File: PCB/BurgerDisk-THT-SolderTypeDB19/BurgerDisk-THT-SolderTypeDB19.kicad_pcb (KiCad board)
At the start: 2 copper layers, 93.7 x 67.6 mm, 17 parts, among them J1 Daisy port in, J2 MicroSD module, J3 UART, J4 Daisy port out, U1 PC817

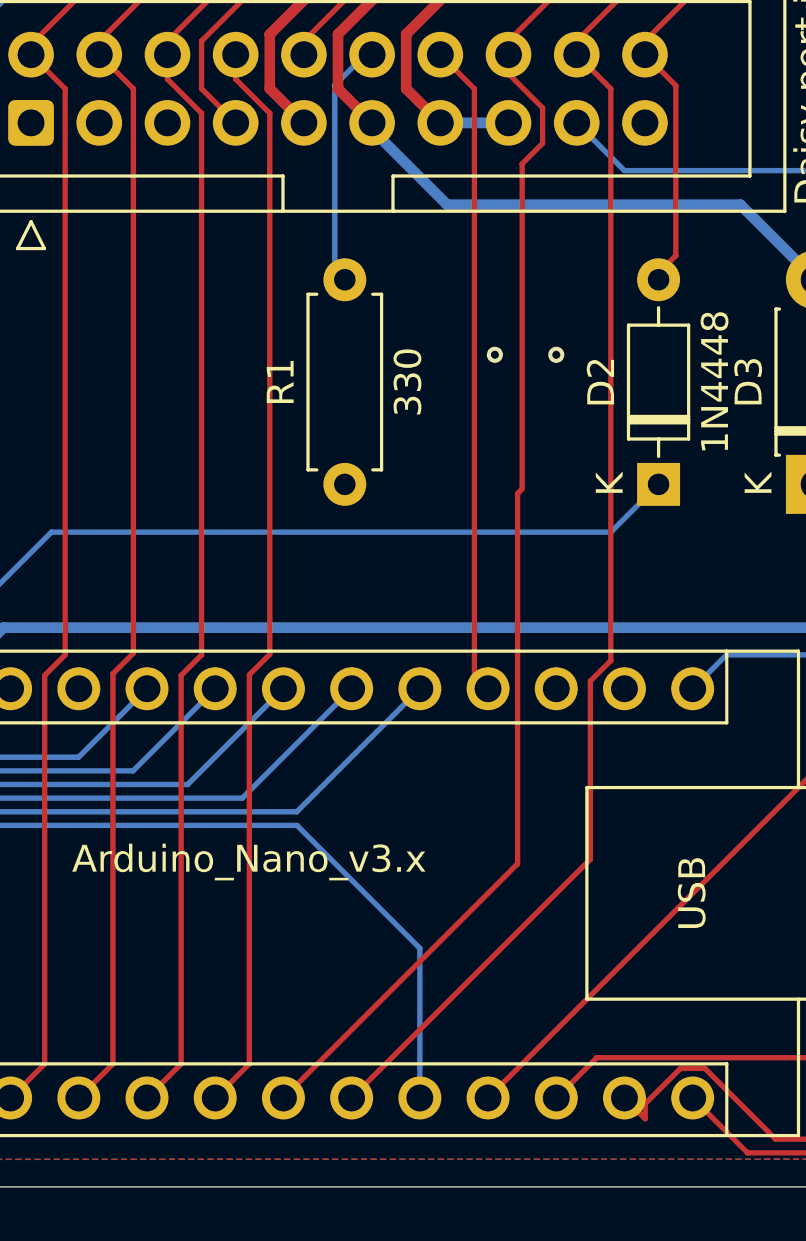
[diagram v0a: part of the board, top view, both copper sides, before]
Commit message: Cleanup PCBs, fatter power traces
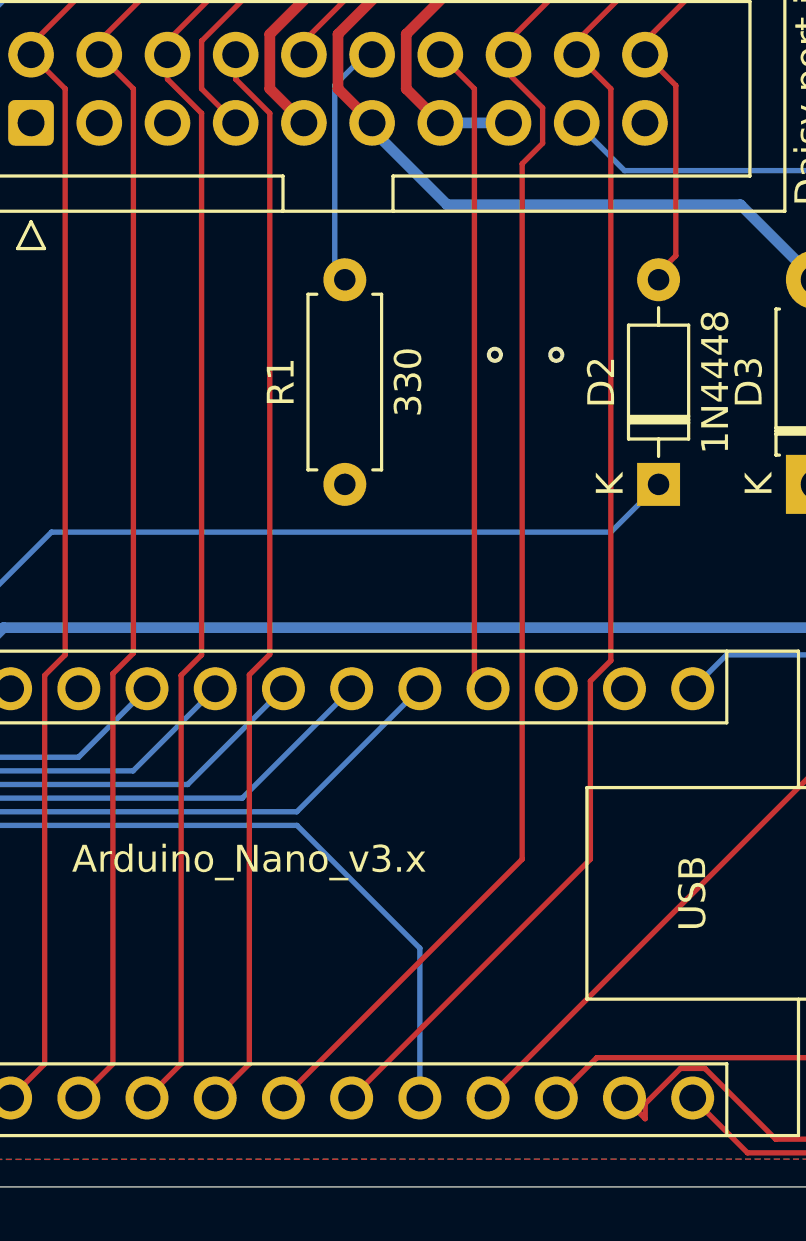
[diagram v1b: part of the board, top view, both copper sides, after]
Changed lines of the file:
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@@
+	)
+	(segment
+		(start 114.808 71.06812)
+		(end 114.808 72.39)
+		(width 0.2)
+		(layer "F.Cu")
+		(net 7)
 	)
 	(segment
@@
 	)
 	(segment
-		(start 113.876 85.428)
-		(end 113.876 99.22)
+		(start 114.046 99.05)
+		(end 105.156 107.94)
+		(width 0.2)
+		(layer "F.Cu")
+		(net 7)
+	)
+	(segment
+		(start 114.046 73.152)
+		(end 114.046 99.05)
+		(width 0.2)
+		(layer "F.Cu")
+		(net 7)
+	)
+	(segment
+		(start 122.936 59.182)
+		(end 113.538 68.58)
+		(width 0.2)
+		(layer "F.Cu")
+		(net 7)
+	)
+	(segment
+		(start 147.574 50.8)
+		(end 139.192 59.182)
+		(width 0.2)
+		(layer "F.Cu")
+		(net 7)
+	)
+	(segment
+		(start 139.192 59.182)
+		(end 122.936 59.182)
 		(width 0.2)
 		(layer "F.Cu")
@@
 	)
 	(segment
-		(start 122.936 59.182)
-		(end 113.538 68.58)
-		(width 0.2)
-		(layer "F.Cu")
-		(net 7)
-	)
-	(segment
-		(start 147.574 50.8)
-		(end 139.192 59.182)
-		(width 0.2)
-		(layer "F.Cu")
-		(net 7)
-	)
-	(segment
 		(start 113.538 69.088)
 		(end 113.538 69.79812)
-		(width 0.2)
-		(layer "F.Cu")
-		(net 7)
-	)
-	(segment
-		(start 139.192 59.182)
-		(end 122.936 59.182)
-		(width 0.2)
-		(layer "F.Cu")
-		(net 7)
-	)
-	(segment
-		(start 114.046 73.152)
-		(end 114.046 85.258)
-		(width 0.2)
-		(layer "F.Cu")
-		(net 7)
-	)
-	(segment
-		(start 114.046 85.258)
-		(end 113.876 85.428)
-		(width 0.2)
-		(layer "F.Cu")
-		(net 7)
-	)
-	(segment
-		(start 113.876 99.22)
-		(end 105.156 107.94)
-		(width 0.2)
-		(layer "F.Cu")
-		(net 7)
-	)
-	(segment
-		(start 114.808 71.06812)
-		(end 114.808 72.39)
 		(width 0.2)
 		(layer "F.Cu")
@@
 		(min_thickness 0.25)
 		(filled_areas_thickness no)
-		(fill yes
+		(fill
 			(thermal_gap 0.5)
 			(thermal_bridge_width 0.5)

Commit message: Let the OCD win
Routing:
- net WRPROT_out: track 55.9 -> 56.5 mm
- net GND: vias 4 -> 27

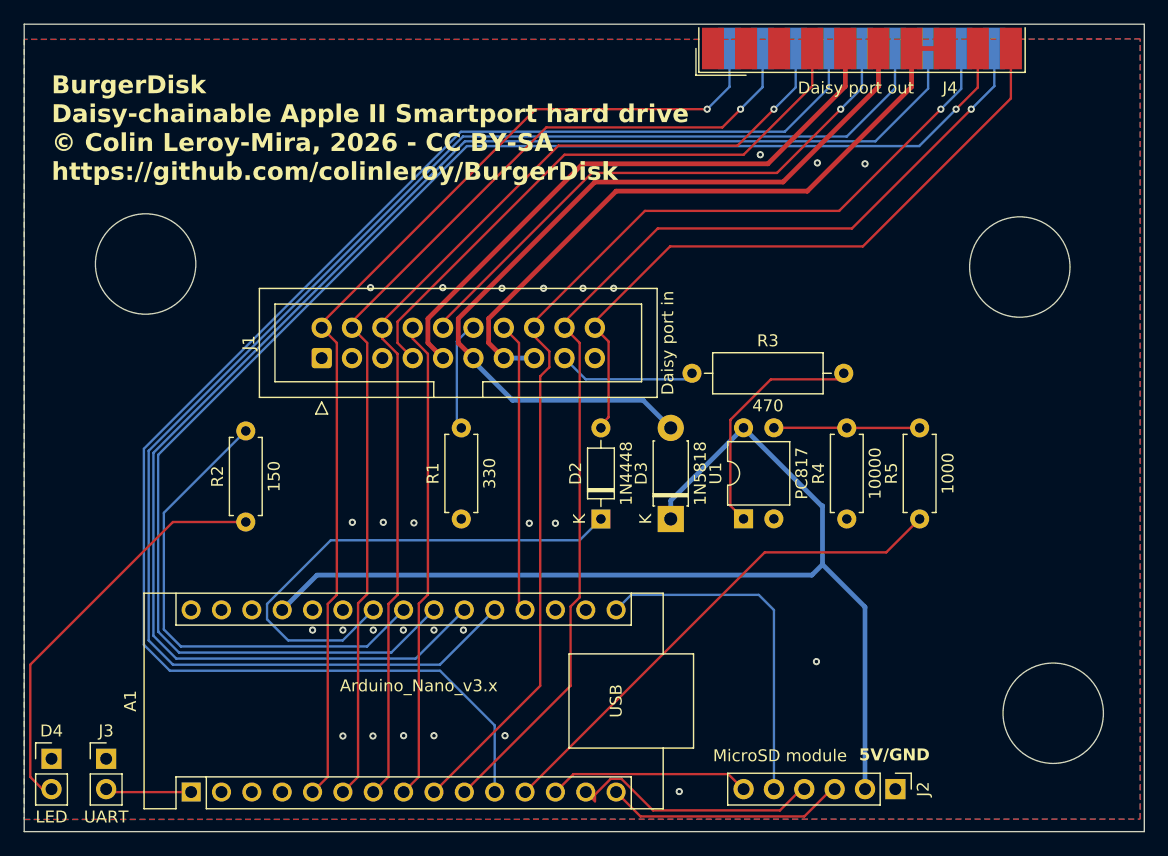
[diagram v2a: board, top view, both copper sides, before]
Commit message: Rework R3 so everything's in line
for easier soldering
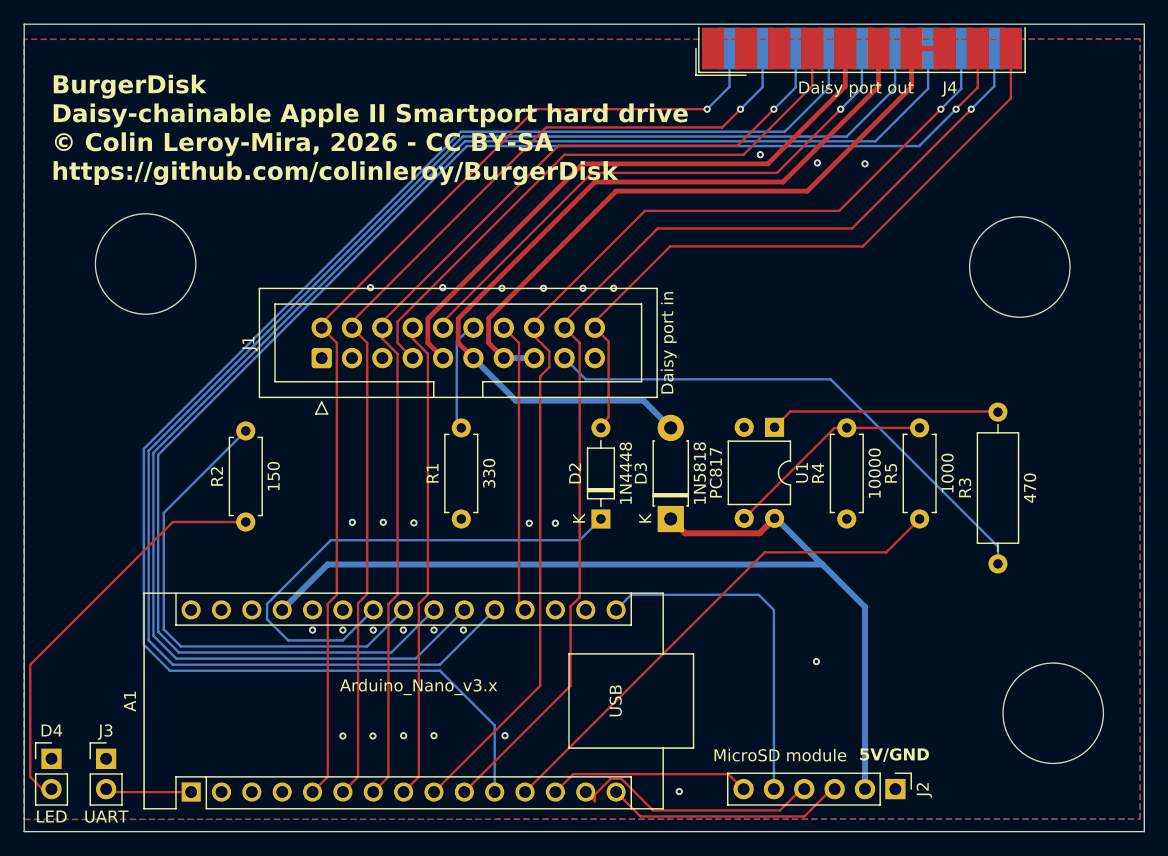
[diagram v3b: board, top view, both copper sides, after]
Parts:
- moved R3 30.2 mm to (152.3, 88.8), turned to 90 degrees
- moved U1 8.09 mm to (133.7, 77.4), turned to -90 degrees
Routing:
- net DRV2_in: track 11.6 -> 44.3 mm
- net 5V_burgerDisk: track 91.4 -> 82.3 mm
- net Net-(R4-Pad2): track 12.2 -> 17.8 mm
- net Net-(R3-Pad2): track 19.8 -> 19.3 mm

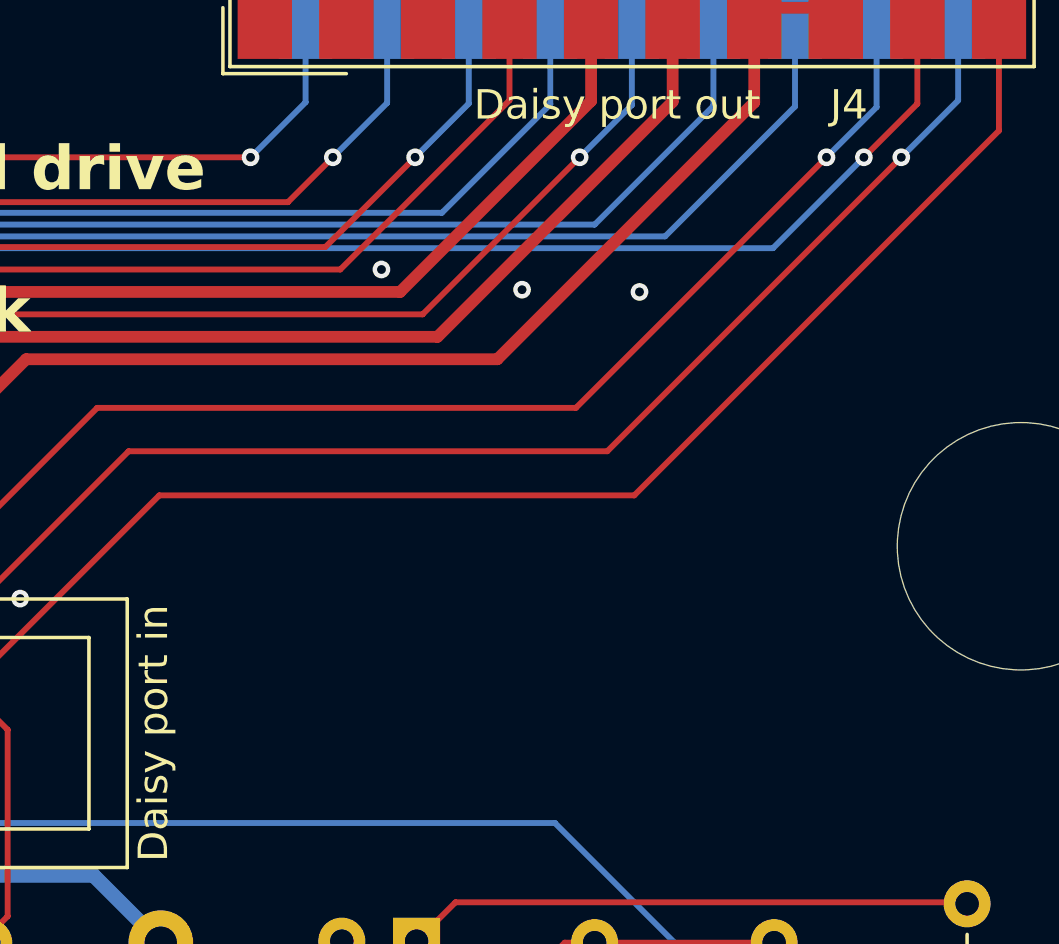
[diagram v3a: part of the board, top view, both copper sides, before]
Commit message: Add logo (thanks to Javier Rivera!!)
Add my own micro/SD modules
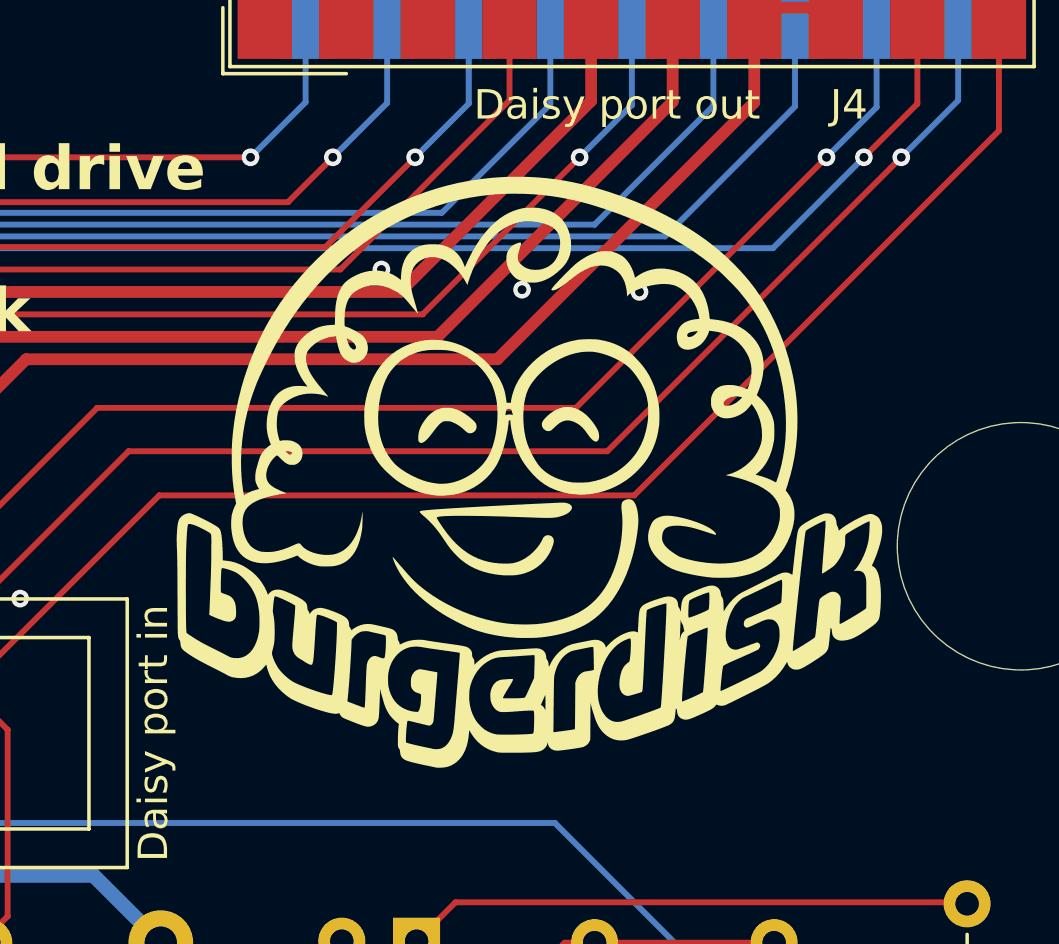
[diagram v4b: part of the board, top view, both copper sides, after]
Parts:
- added G***: LOGO, LOGO, F.Cu at (137.5, 61.6)

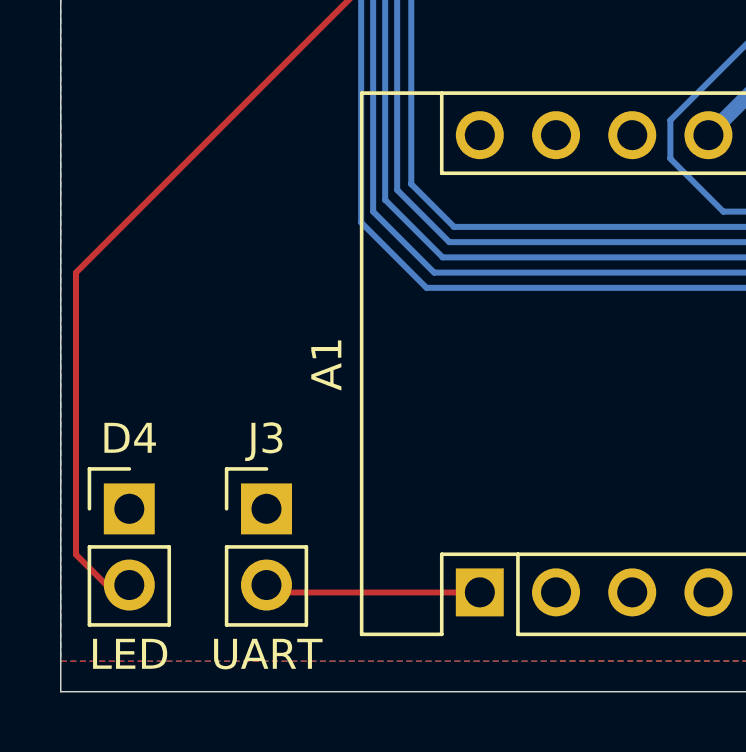
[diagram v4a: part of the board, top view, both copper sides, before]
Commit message: Small caps fixes
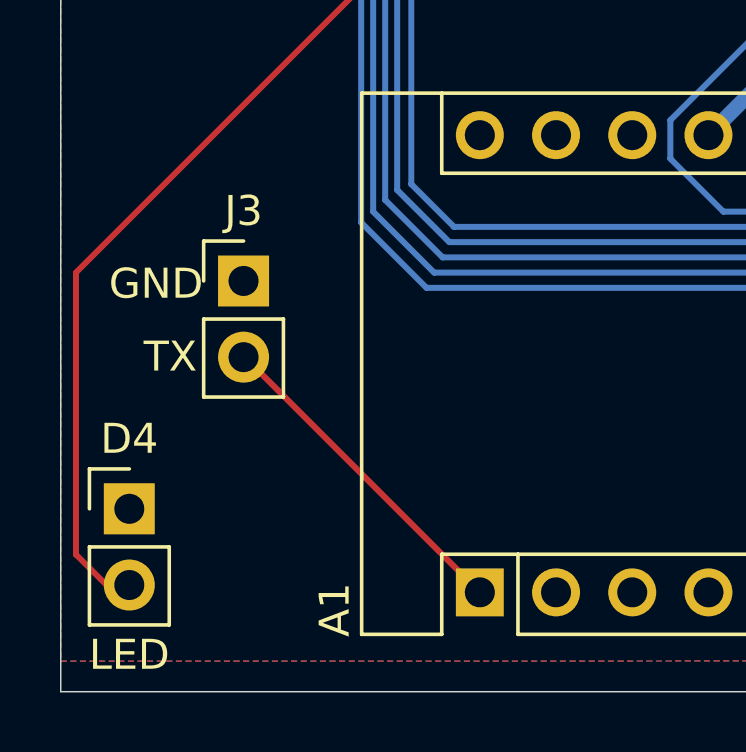
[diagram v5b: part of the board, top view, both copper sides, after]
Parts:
- moved J3 7.63 mm to (77.0, 97.6)
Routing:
- net TX: track 7.22 -> 11.1 mm
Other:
- board text added: "GND"
- board text added: "TX"
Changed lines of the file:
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@@
 	(footprint "Connector_PinHeader_2.54mm:PinHeader_1x02_P2.54mm_Vertical"
 		(layer "F.Cu")
-		(at 77.724 105.156)
+		(at 76.96 97.56)
 		(descr "Through hole straight pin header, 1x02, 2.54mm pitch, single row")
 		(tags "Through hole pin header THT 1x02 2.54mm single row")
@@
 		(property "Value" "UART"
 			(at 0 4.87 0)
-			(layer "F.SilkS")
+			(layer "F.Fab")
 			(effects
 				(font
@@
 		(tags "Arduino Nano")
 		(property "Reference" "A1"
-			(at 7.62 -5.08 90)
+			(at -0.58 -4.836 90)
 			(layer "F.SilkS")
 			(effects
@@
 		)
 	)
+	(gr_text "TX"
+		(at 73.63 100.67 0)
+		(layer "F.SilkS")
+		(effects
+			(font
+				(size 1 1)
+				(thickness 0.1)
+			)
+			(justify left bottom)
+		)
+	)
+	(gr_text "GND"
+		(at 72.47 98.24 0)
+		(layer "F.SilkS")
+		(effects
+			(font
+				(size 1 1)
+				(thickness 0.1)
+			)
+			(justify left bottom)
+		)
+	)
 	(dimension
 		(type aligned)
@@
 	)
 	(segment
-		(start 77.724 107.696)
-		(end 77.973 107.945)
+		(start 76.96 100.1)
+		(end 77 100.1)
 		(width 0.2)
 		(layer "F.Cu")
@@
 	)
 	(segment
-		(start 77.973 107.945)
-		(end 84.831 107.945)
+		(start 77 100.1)
+		(end 84.831 107.931)
 		(width 0.2)
 		(layer "F.Cu")
@@
 		(width 0.2)
 		(layer "F.Cu")
+		(net 1)
+	)
+	(segment
+		(start 84.831 107.931)
+		(end 84.831 107.945)
+		(width 0.2)
+		(layer "F.Cu")

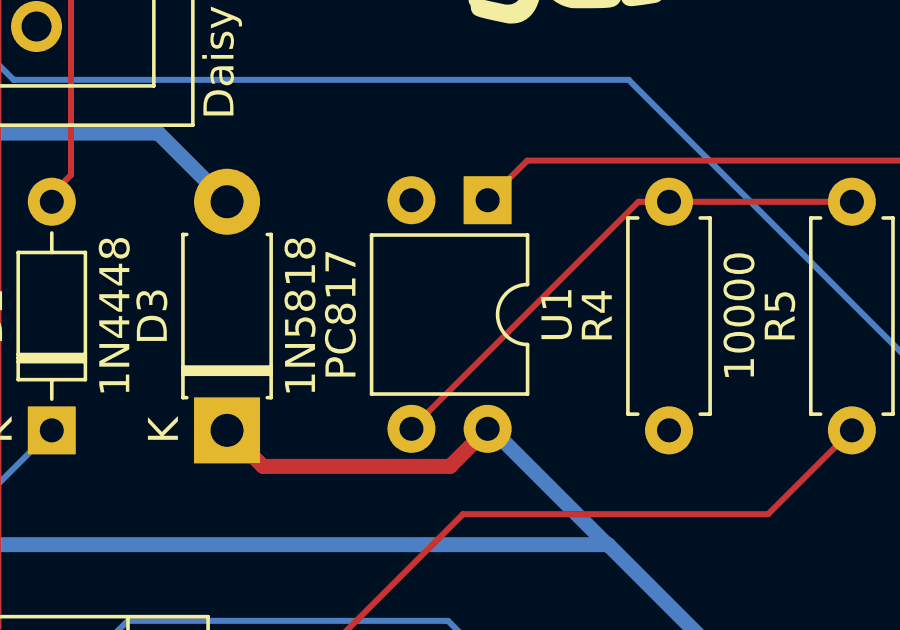
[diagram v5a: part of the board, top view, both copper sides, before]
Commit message: Enable teardrops
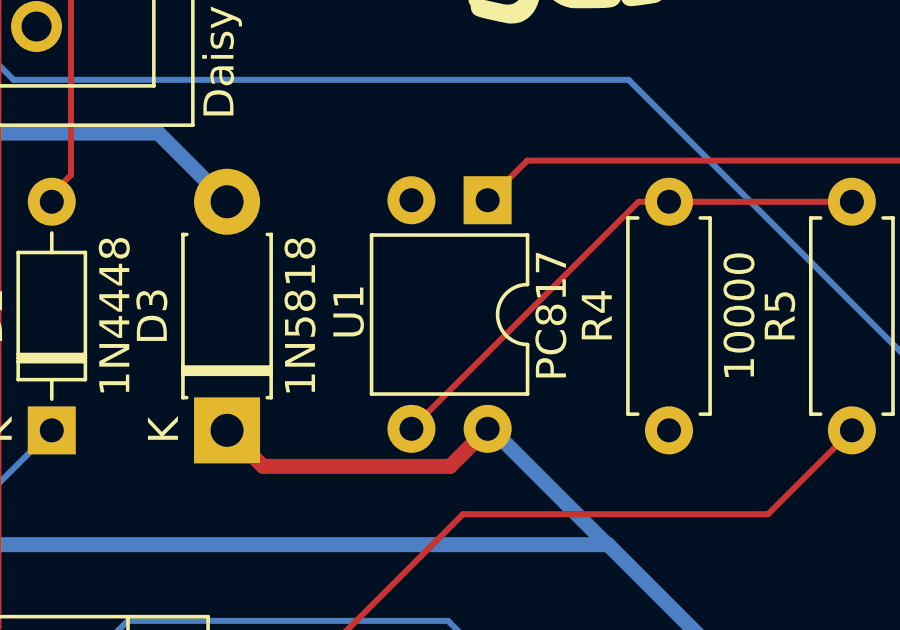
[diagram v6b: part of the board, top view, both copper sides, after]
